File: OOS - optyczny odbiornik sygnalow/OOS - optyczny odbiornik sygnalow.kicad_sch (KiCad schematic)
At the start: 37 parts, among them J101 Conn_Coaxial, J102 Conn_01x02_Socket, J103 Conn_01x02_Socket, J104 Conn_01x02_Socket, J105 Conn_01x02_Socket, U101 OPA300AIDBVR, U102 OPA300AIDBVR

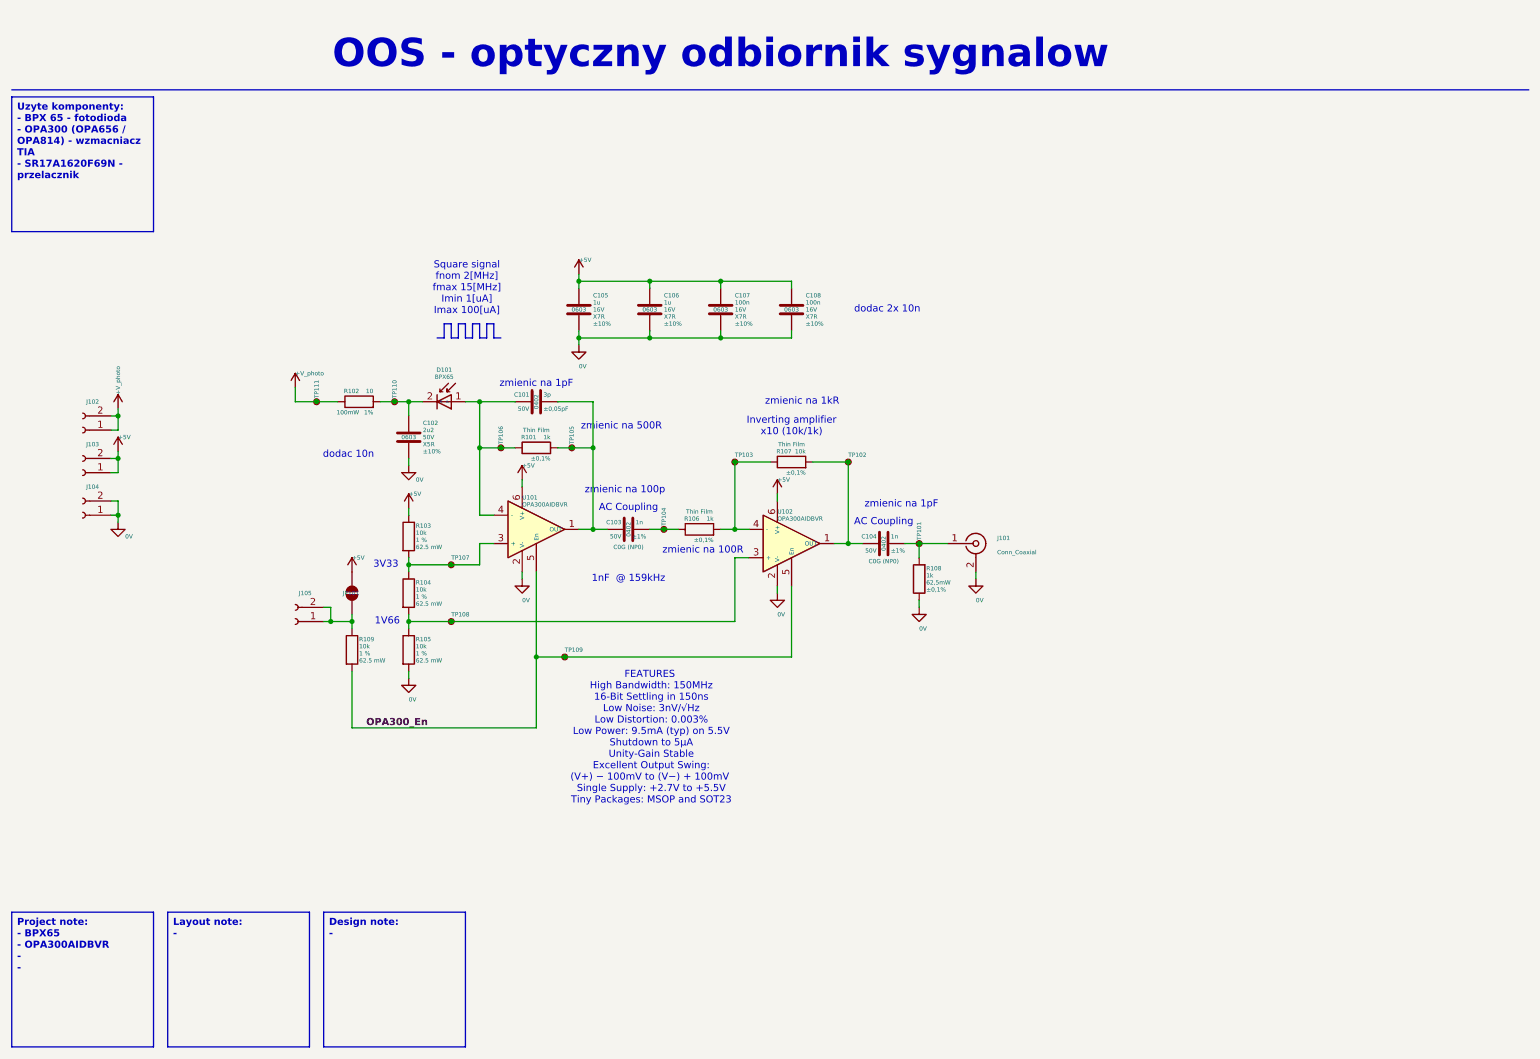
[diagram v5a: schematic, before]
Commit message: Przesuniecie komentarza
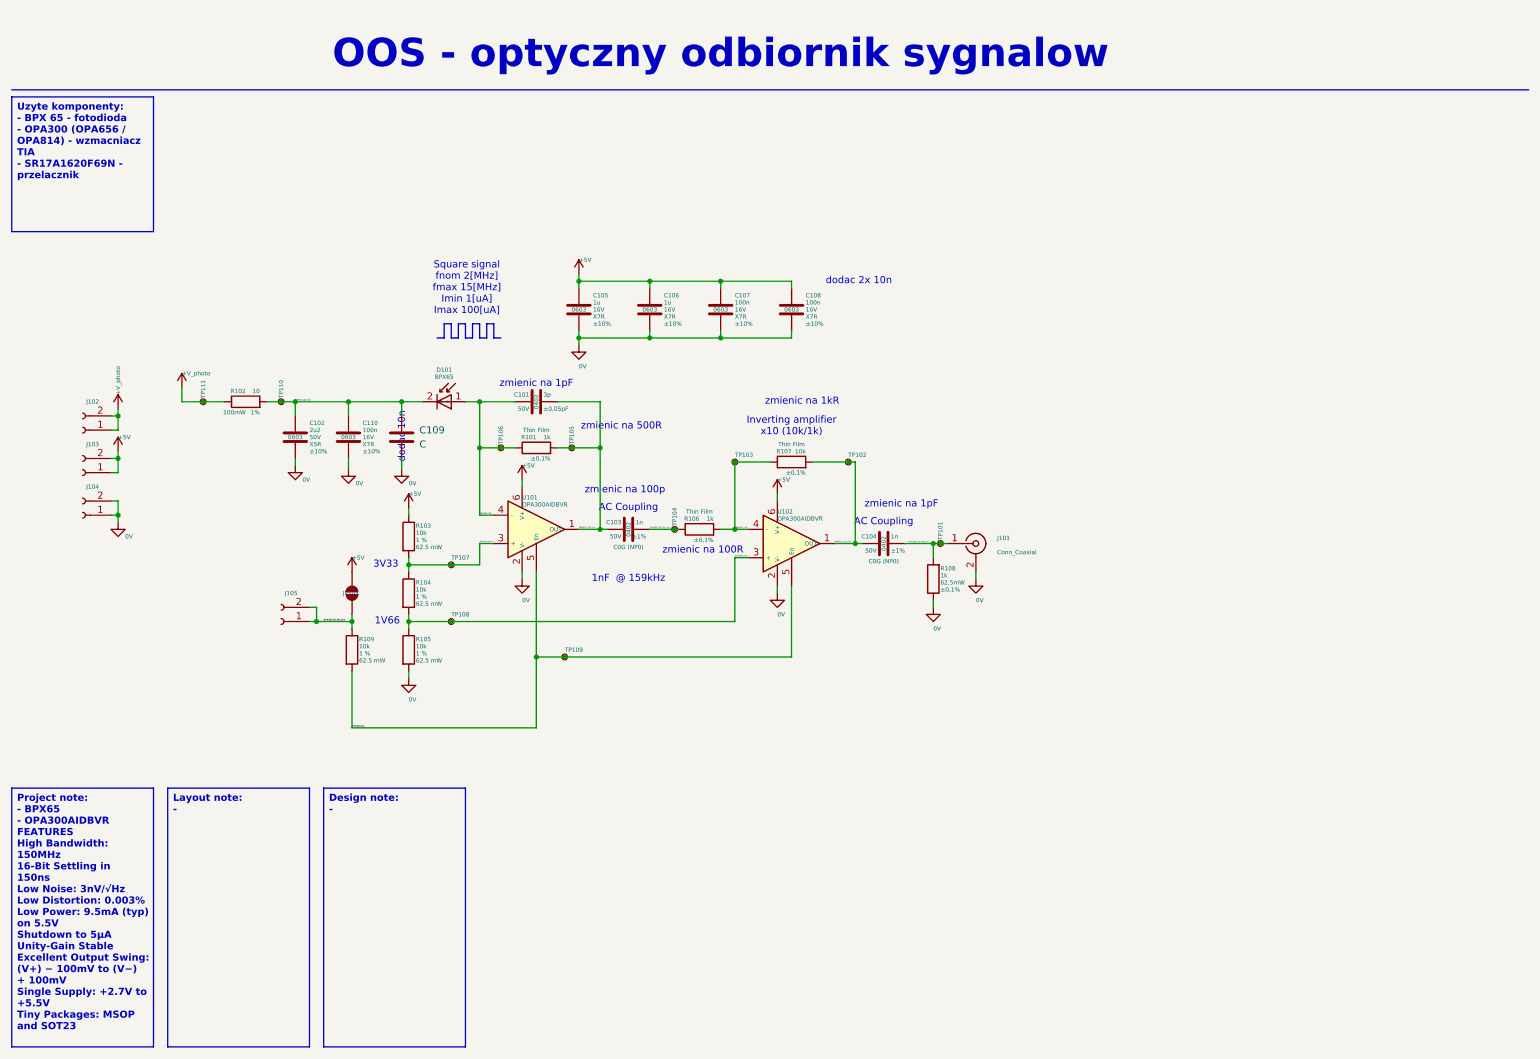
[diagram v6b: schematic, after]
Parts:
- added C109: C, symbol Device:C
- added C110: 100n, Resistor_SMD:R_0603_1608Metric, symbol Device:C
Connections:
- net 0V: now also C109.2, C110.2
- net BPX65_Cathode: now reaches C102.2, D101.2 (K), R102.2, TP110.1
- net BPX65_Cathode: now also C109.1, C110.1
- net OPA300_En_Alt_Con: now reaches J105.1 (Pin_1), J105.2 (Pin_2), JP101.1 (A), R109.1
- net OPA300_TIA_-: now reaches C101.1, D101.1 (A), R101.1, TP106.1, U101.4 (-)
- net OPA300_TIA_Out: now reaches C101.2, C103.1, R101.2, TP105.1, U101.1 (OUT)
- net OPA300_x10_Out_AC: now reaches C104.2, J101.1 (In), R108.2, TP101.1
- net OPA300_TIA_+: now reaches R103.2, R104.1, TP107.1, U101.3 (+)
- net OPA300_x10_+: now reaches R104.2, R105.1, TP108.1, U102.3 (+)
- net OPA300_x10_Out: now reaches C104.1, R107.2, TP102.1, U102.1 (OUT)
- net OPA300_TIA_Out_AC: now reaches C103.2, R106.1, TP104.1
- net OPA300_x10_-: now reaches R106.2, R107.1, TP103.1, U102.4 (-)
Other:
- note removed: "FEATURES High Bandwidth: 150MHz 16-Bit Settling in 150ns Low Noise: 3nV/√Hz Low Distortion: 0.003% Low Power: 9.5mA (typ) on 5.5V Shutdown to 5μA Unity-Gain Stable Excellent Output Swing: (V+) − 100mV to (V−) + 100mV Single Supply: +2.7V to +5.5V Tiny Packages: MSOP and SOT23"
- moved on the sheet: C102, J105, R102, R108, TP101, TP104, TP110, TP111

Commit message: Poprawa na schemacie, dodanie otworów i pozycjonerow, wczytanie komponentow na pcb
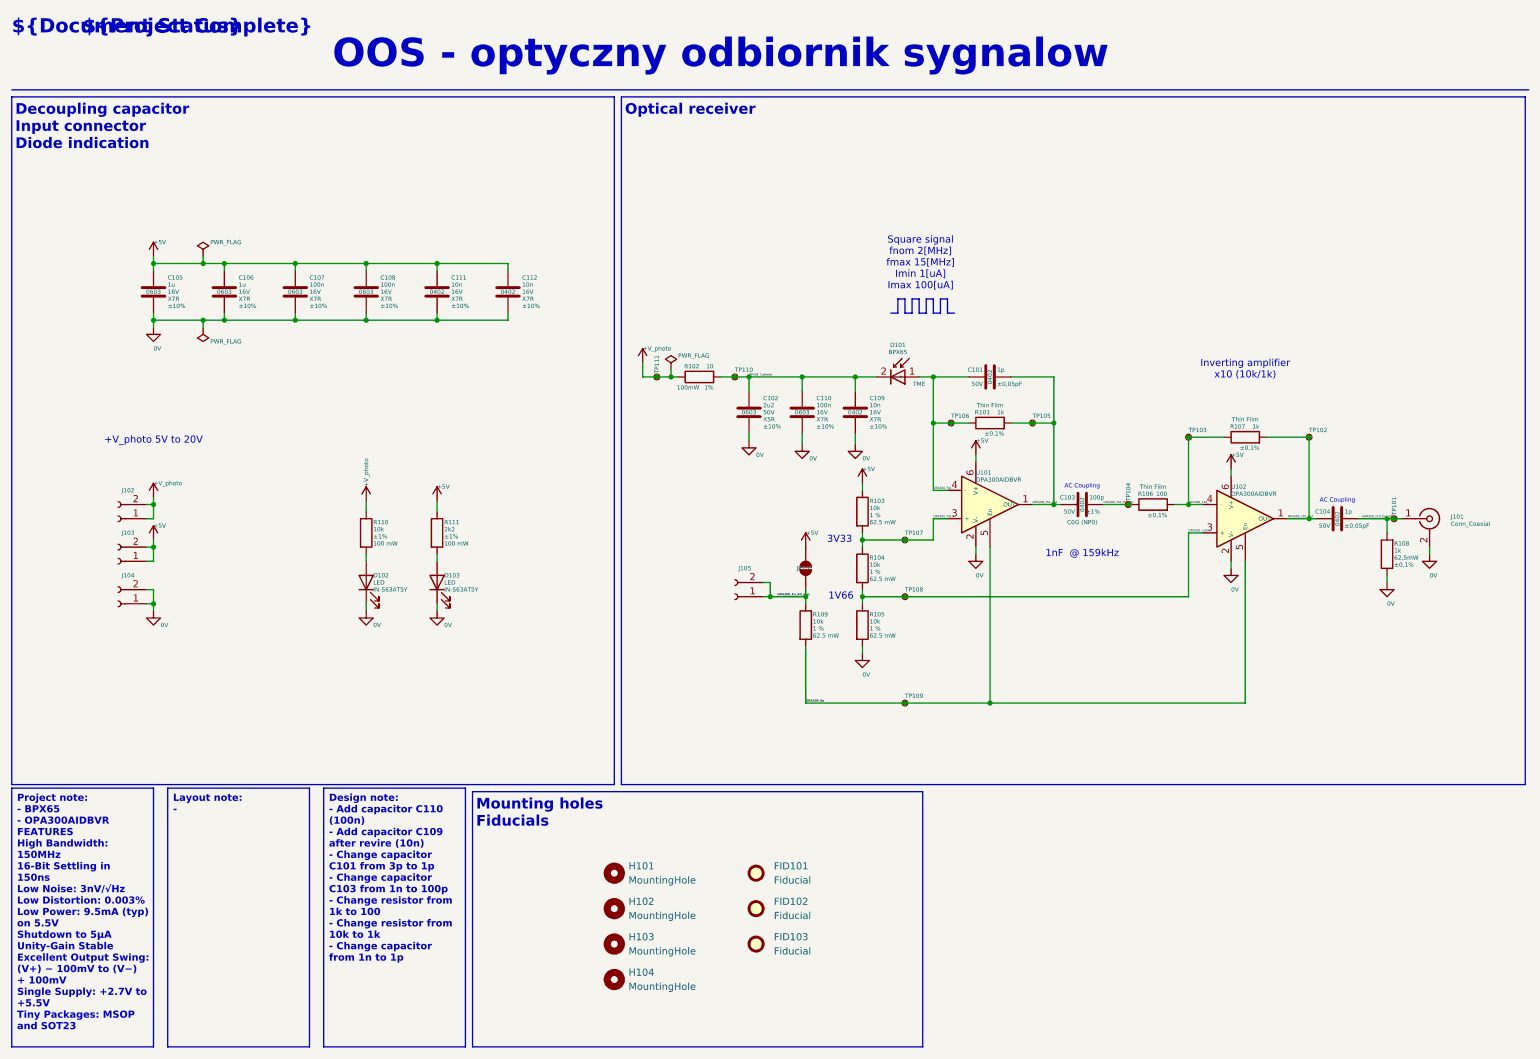
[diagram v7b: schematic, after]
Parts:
- added C111, C112: 10n, Capacitor_SMD:C_0402_1005Metric, symbol Device:C
- added D102, D103: LED, Diode_SMD:D_0603_1608Metric, symbol Device:LED
- added FID101, FID102, FID103: Fiducial, Fiducial:Fiducial_1.5mm_Mask3mm, symbol Mechanical:Fiducial
- added H101, H102, H103, H104: MountingHole, MountingHole:MountingHole_3.2mm_M3, symbol Mechanical:MountingHole
- added R110: 10k, Resistor_SMD:R_0603_1608Metric, symbol Device:R
- added R111: 2k2, Resistor_SMD:R_0603_1608Metric, symbol Device:R
- C101: value 3p -> 1p; Dielectric (none) -> COG (NP0); MPN GJM1555C1H3R0WB01D -> (none); MPN after review (none) -> GJM1555C1H1R0WB01D; MPN before review (none) -> GJM1555C1H3R0WB01D
- C102: footprint Capacitor_SMD:C_0402_1005Metric -> Capacitor_SMD:C_0603_1608Metric; MPN LMK107BJ225KA-T -> (none); MPN after review (none) -> LMK107BJ225KA-T; Supplier Digi Key -> NA
- C103: value 1n -> 100p; MPN GCM1555C1H102FA16 -> (none); MPN after review (none) -> GCM1555C1H101FA16D; MPN before review (none) -> GCM1555C1H102FA16; Supplier (none) -> TME
- C104: value 1n -> 1p; MPN GCM1555C1H102FA16 -> (none); MPN after review (none) -> GJM1555C1H1R0WB01D; MPN before review (none) -> GCM1555C1H102FA16; Supplier (none) -> TME; Tolerance ±1% -> ±0,05pF
- C105, C106: MPN C0603C105K4RACTU -> (none); MPN after review (none) -> C0603C105K4RACTU; Supplier (none) -> TME
- C107, C108, C110: MPN EMK108B7104KA-T -> (none); MPN after review (none) -> EMK108B7104KA-T; Supplier (none) -> TME
- C109: value C -> 10n; footprint (none) -> Capacitor_SMD:C_0402_1005Metric; Dielectric (none) -> X7R; MPN after review (none) -> CL05B103KO5NNNC; Package (none) -> 0402; Supplier (none) -> TME; Tolerance (none) -> ±10%; Voltage Rating (none) -> 16V
- D101: footprint (none) -> Package_TO_SOT_THT:TO-18-2_Lens; Supplier (none) -> TME
- J101: footprint (none) -> Connector_Coaxial:BNC_Amphenol_B6252HB-NPP3G-50_Horizontal; Supplier (none) -> TME
- JP101: footprint (none) -> Jumper:SolderJumper-2_P1.3mm_Bridged_RoundedPad1.0x1.5mm
- R101, R108: MPN RT0402BRD071KL -> (none); MPN after review (none) -> RT0402BRD071KL
- R102: Supplier (none) -> TME
- R103, R104, R105, R109: MPN RC0603JR-13100KL -> (none); MPN after review (none) -> RC0603JR-13100KL; Supplier (none) -> TME
- R106: value 1k -> 100; MPN RT0402BRD071KL -> (none); MPN after review (none) -> ERA2AEB101X; MPN before review (none) -> RT0402BRD071KL; Package (none) -> 0402; Supplier (none) -> TME; Voltage Rating (none) -> 100V
- R107: value 10k -> 1k; MPN RT0402BRD0710KL -> (none); MPN after review (none) -> RT0402BRD071KL; MPN before review (none) -> RT0402BRD0710KL; Power Rating 62.5 mW -> 62,5mW
- U101, U102: footprint (none) -> Package_TO_SOT_SMD:SOT-23-6_Handsoldering; Supplier (none) -> TME
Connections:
- net +5V: now also C111.1, C112.1, R111.1
- net +V_photo: now also R110.1
- net 0V: now also C111.2, C112.2, D102.1 (K), D103.1 (K)
- new net: D103.2 (A), R111.2
- new net: D102.2 (A), R110.2
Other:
- note added: "${Document Status}"
- note added: "${Project Complete}"
- note added: "+V_photo 5V to 20V"
- note added: "Decoupling capacitor Input connector Diode indication"
- note added: "Mounting holes Fiducials"
- note added: "Optical receiver"
- note removed: "dodac 10n"
- note removed: "dodac 2x 10n"
- note removed: "zmienic na 100R"
- note removed: "zmienic na 100p"
- note removed: "zmienic na 1kR"
- note removed: "zmienic na 1pF"
- note removed: "zmienic na 500R"
- company: (none) -> ${Company}
- title: (none) -> ${Project Title}
- moved on the sheet: C101, C102, C105, C106, C107, C108, C109, C110, D101, J101, J102, J103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

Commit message: Polozenei komponentow na plycie, zdefiniowanie geometri, wczesny layout
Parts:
- renumbered C105 to C1, C101 to C10, C103 to C11, C104 to C12, C106 to C2, C107 to C3, C108 to C4, C111 to C5, C112 to C6, C102 to C7, C110 to C8, C109 to C9, D102 to D1, D103 to D2, D101 to D3, FID101 to FID1, FID102 to FID2, FID103 to FID3, H101 to H1, H102 to H2, H103 to H3, H104 to H4, J102 to J1, J103 to J2, J104 to J3, J105 to J4, J101 to J5, JP101 to JP1, R110 to R1, R107 to R10, R108 to R11, R111 to R2, R102 to R3, R109 to R4, R103 to R5, R104 to R6, R105 to R7, R101 to R8, R106 to R9, TP111 to TP1, TP102 to TP10, TP101 to TP11, TP110 to TP2, TP107 to TP3, TP108 to TP4, TP109 to TP5, TP106 to TP6, TP105 to TP7, TP104 to TP8, TP103 to TP9, U101 to U1, U102 to U2
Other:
- note removed: "1nF @ 159kHz"
